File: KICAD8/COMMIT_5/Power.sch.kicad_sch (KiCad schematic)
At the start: 50 parts, among them J2 USB_B_Micro, U1 BAS16HT1G, U4 USBLC6-2SC6

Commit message: In-progress Changes
HVT 1 -> 2, switching to a different format without pyro system. In between development, issues with HVT 1 from manufacturer, one from my design.
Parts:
- removed 3v3: 3v3, TestPoint:TestPoint_Pad_1.5x1.5mm, symbol Connector:TestPoint
- removed 5v1: 5V, TestPoint:TestPoint_Pad_1.5x1.5mm, symbol Connector:TestPoint
- removed BOOT0, NRST1: OS102011MS2QN1, OS102011MS2QN1:SW_OS102011MS2QN1, symbol OS102011MS2QN1:OS102011MS2QN1
- removed C29: 100nF, Capacitor_SMD:C_0805_2012Metric, symbol Device:C
- removed D4: YELLOW, LED_SMD:LED_0805_2012Metric, symbol cr-2032:LED
- removed R12, R14: 10k, Resistor_SMD:R_0805_2012Metric, symbol Device:R
- removed R13: 100, Resistor_SMD:R_0805_2012Metric, symbol Device:R
- removed S1: SERVO1, TestPoint:TestPoint_Pad_1.5x1.5mm, symbol Connector:TestPoint
- removed S2: SERVO2, TestPoint:TestPoint_Pad_1.5x1.5mm, symbol Connector:TestPoint
- removed S3: SERVO3, TestPoint:TestPoint_Pad_1.5x1.5mm, symbol Connector:TestPoint
- removed S4: SERVO4, TestPoint:TestPoint_Pad_1.5x1.5mm, symbol Connector:TestPoint
- removed S5: SERVO5, TestPoint:TestPoint_Pad_1.5x1.5mm, symbol Connector:TestPoint
- removed SWCLK1: SWCLK, TestPoint:TestPoint_Pad_1.5x1.5mm, symbol Connector:TestPoint
- removed Vbatbkp1: Vbckp, TestPoint:TestPoint_Pad_1.5x1.5mm, symbol Connector:TestPoint
- added R21, R22: 0, Resistor_SMD:R_0805_2012Metric_Pad1.20x1.40mm_HandSolder, symbol Device:R_Small
- C10, C11, C12, C13, C14, C28, C31, C5, C6, C7, C8, C9: footprint Capacitor_SMD:C_0805_2012Metric -> Capacitor_SMD:C_0805_2012Metric_Pad1.18x1.45mm_HandSolder
- C15, C27: footprint Capacitor_SMD:C_0603_1608Metric -> Capacitor_SMD:C_0805_2012Metric_Pad1.18x1.45mm_HandSolder
- C52: footprint Capacitor_SMD:C_0201_0603Metric -> Capacitor_SMD:C_0805_2012Metric_Pad1.18x1.45mm_HandSolder
- D1, D2: footprint LED_SMD:LED_0805_2012Metric -> LED_SMD:LED_0805_2012Metric_Pad1.15x1.40mm_HandSolder
- R1, R3, R4: footprint Resistor_SMD:R_0603_1608Metric -> Resistor_SMD:R_0805_2012Metric_Pad1.20x1.40mm_HandSolder
- R2: footprint Resistor_SMD:R_0805_2012Metric -> Resistor_SMD:R_0805_2012Metric_Pad1.20x1.40mm_HandSolder
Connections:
- net 5v-out: now also R21.1; no longer D5.2 (A)
- net VBAT_SWITCH: now also R22.2; no longer 5VReg1.2 (Vin), 5VReg1.3 (EN), C12.1, R2.1
- new net: D5.2 (A), R21.2
- new net: 5VReg1.2 (Vin), 5VReg1.3 (EN), C12.1, R2.1, R22.1
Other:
- note removed: "BOOT-SWITCH"
- note removed: "NRST-SWITCH"
- note removed: "Test Points"

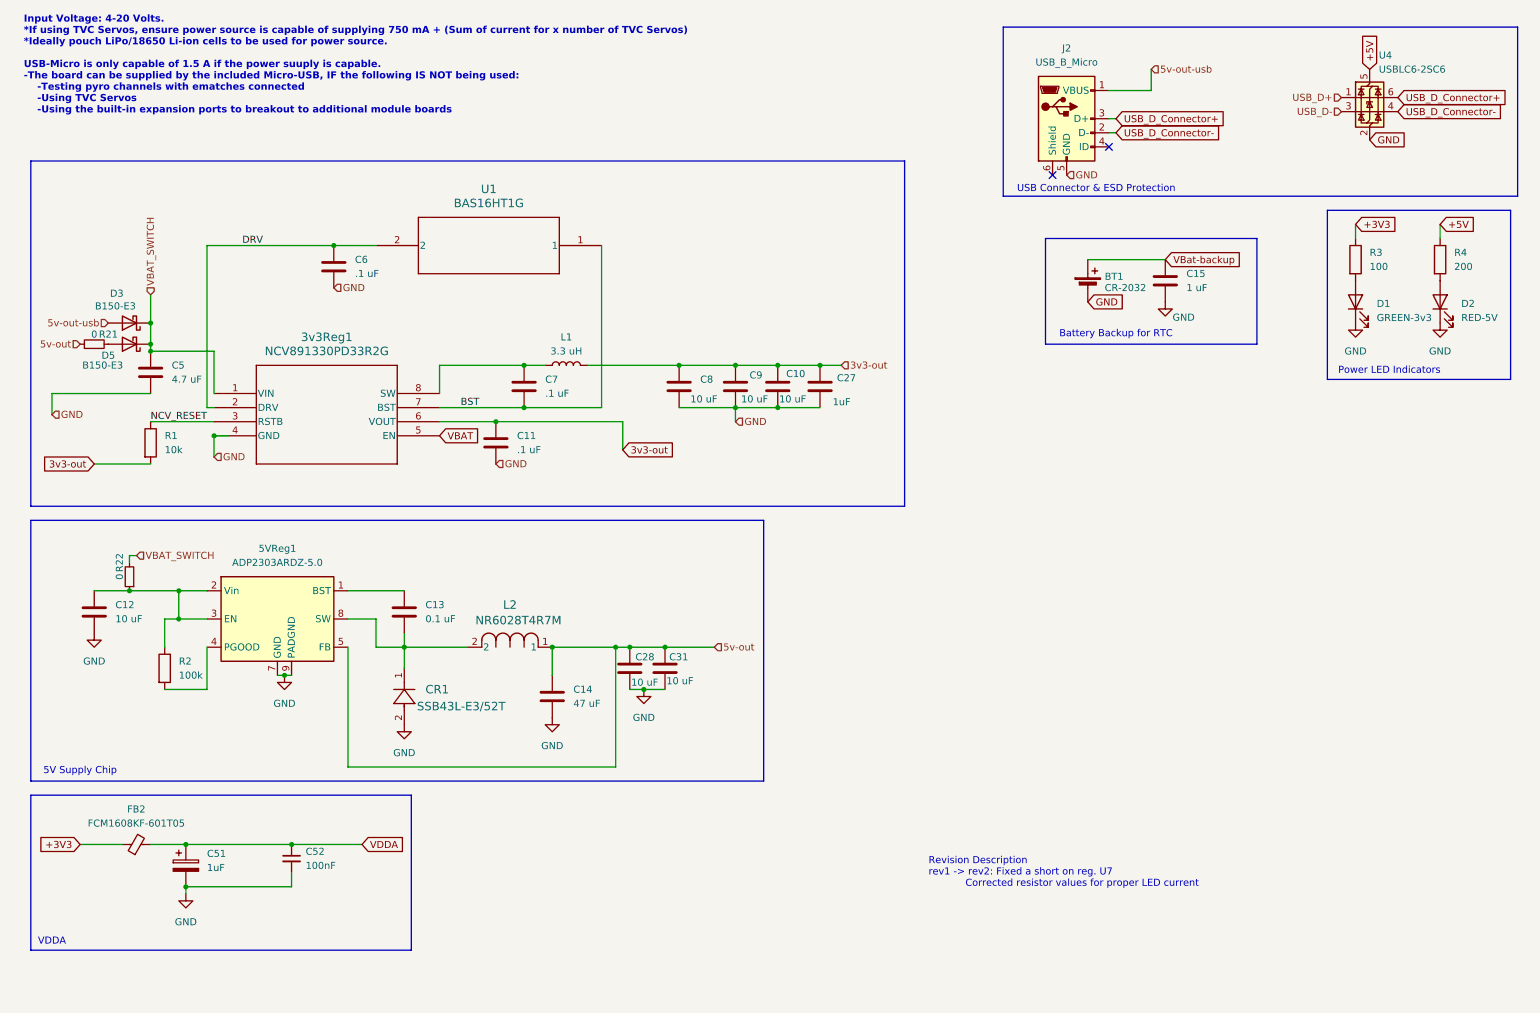
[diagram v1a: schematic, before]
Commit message: Intermediary Progress on HVT2
Removed pyro circuits for cost reasons, most of layout completed, traces need to be routed still
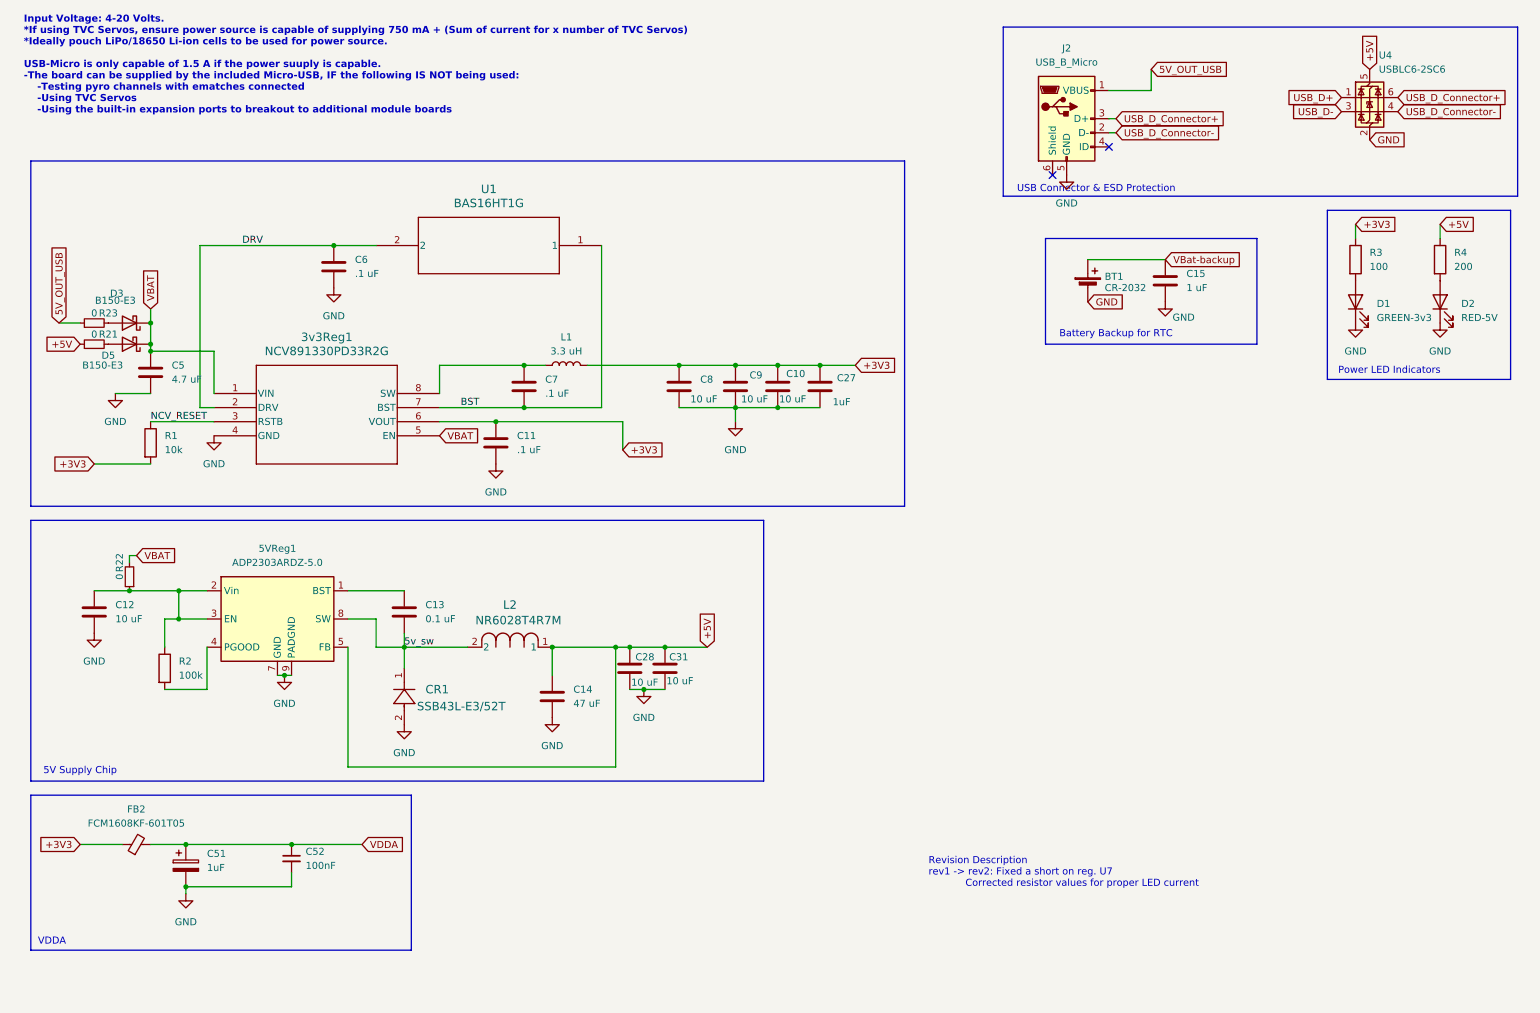
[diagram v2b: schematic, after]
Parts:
- added R23: 0, Resistor_SMD:R_0805_2012Metric_Pad1.20x1.40mm_HandSolder, symbol Device:R_Small
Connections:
- net 3v3-out is gone; now on net +3V3: 3v3Reg1.6 (VOUT), C10.1, C11.1, C27.1, C8.1, C9.1, L1.2, R1.2
- net 5v-out is gone; now on net +5V: 5VReg1.5 (FB), C14.1, C28.1, C31.1, L2.1, R21.1
- net VBAT_SWITCH is gone; now on net VBAT: 3v3Reg1.1 (VIN), C5.1, D3.1 (K), D5.1 (K), R22.2
- net 5v_sw: now reaches 5VReg1.8 (SW), C13.2, CR1.1, L2.2
- net 5v-out-usb: no longer names the net of D3.2 (A)
- net 5v-out-usb: now also R23.2; no longer J2.1 (VBUS)
- new net 5V_OUT_USB: J2.1 (VBUS), R23.1

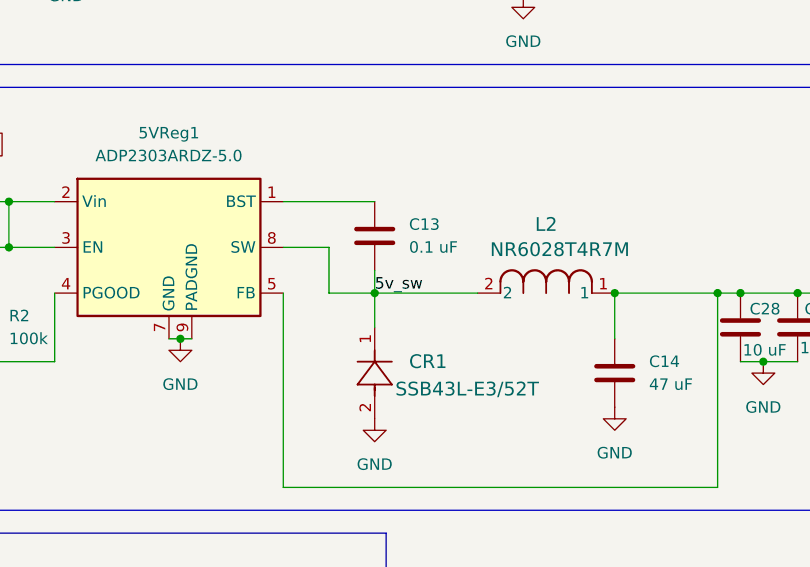
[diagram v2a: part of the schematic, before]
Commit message: HVT2-No Traces
HVT2 layout complete, no traces yet
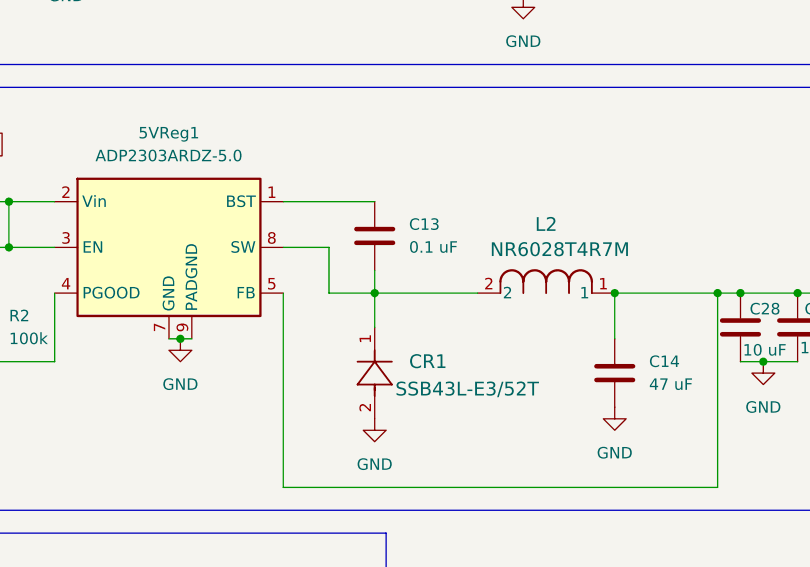
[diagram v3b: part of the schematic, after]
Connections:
- net 5v_sw: no longer names the net of 5VReg1.8 (SW), C13.2, CR1.1, L2.2
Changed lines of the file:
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@@
-		)
-	)
-	(label "5v_sw"
-		(at 83.82 129.54 0)
-		(fields_autoplaced yes)
-		(effects
-			(font
-				(size 1.27 1.27)
-			)
-			(justify left bottom)
 		)
 	)
